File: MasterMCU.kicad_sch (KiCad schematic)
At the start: 0 parts

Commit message: STM32 pinout
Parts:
- added C201, C205, C206, C207, C208, C210, C212, C213, C214: 100n, Capacitor_SMD:C_0805_2012Metric, symbol Device:C
- added C202, C203, C216, C218: 6p, Capacitor_SMD:C_0805_2012Metric, symbol Device:C
- added C204: 10u, Capacitor_SMD:C_0805_2012Metric, symbol Device:C
- added C209, C211, C215, C217: 2u2, Capacitor_SMD:C_0805_2012Metric, symbol Device:C
- added FB201: 90R, Resistor_SMD:R_0805_2012Metric, symbol Device:FerriteBead
- added R201, R202: 100k, Resistor_SMD:R_0805_2012Metric, symbol Device:R_US
- added R203, R204, R205, R206: 22R, symbol Device:R_US
- added SW201: RST, Button_Switch_SMD:SW_SPST_B3U-1000P, symbol Switch:SW_SPST
- added SW202: BOOT, Button_Switch_SMD:SW_SPST_B3U-1000P, symbol Switch:SW_SPST
- added U201: STM32H7B0VBTx, Package_QFP:LQFP-100_14x14mm_P0.5mm, symbol MCU_ST_STM32H7:STM32H7B0VBTx
- added Y201: 16MHz, Crystal:Crystal_SMD_EuroQuartz_MT-4Pin_3.2x2.5mm, symbol Device:Crystal_GND24
- added Y202: 32.768kHZ, Crystal:Crystal_SMD_SeikoEpson_MC306-4Pin_8.0x3.2mm, symbol Device:Crystal_GND23
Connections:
- new net: R205.2, U201.3 (PE4)
- new net: R204.2, U201.1 (PE2)
- new net: C214.1, C215.1, FB201.1, U201.21 (VDDA)
- new net: C209.1, U201.48 (VCAP)
- new net: R206.2, U201.5 (PE6)
- new net: C211.1, U201.73 (VCAP)
- new net: R203.1, U201.78 (PC10)
- new net +3.3V: C204.1, C205.1, C206.1, C207.1, C208.1, C210.1, C212.1, C213.1, C217.1, FB201.2, R201.1, SW202.2 (B), U201.100 (VDD), U201.11 (VDD), U201.27 (VDD), U201.50 (VDD), U201.6 (VBAT), U201.75 (VDD)
- new net BCK_C: R203.2
- new net BOOT0: R202.1, SW202.1 (A), U201.94 (BOOT0)
- new net DOUT_C: U201.79 (PC11)
- new net GND: C201.2, C202.1, C203.1, C204.2, C205.2, C206.2, C207.2, C208.2, C209.2, C210.2, C211.2, C212.2, C213.2, C214.2, C215.2, C216.2, C217.2, C218.2, R202.2, SW201.1 (A), U201.10 (VSS), U201.19 (VSSA), U201.26 (VSS), U201.49 (VSS), U201.74 (VSS), U201.99 (VSS), Y201.2, Y201.4, Y202.2, Y202.3
- new net HSE_IN: C203.2, U201.12 (PH0), Y201.3
- new net HSE_OUT: C202.2, U201.13 (PH1), Y201.1
- new net LFE_IN: C216.1, U201.9 (PC15), Y202.1
- new net LFE_OUT: C218.1, U201.8 (PC14), Y202.4
- new net LORA_BUSY: U201.97 (PE0)
- new net LORA_IRQ: U201.98 (PE1)
- new net LORA_MISO: U201.4 (PE5)
- new net LORA_MOSI: R206.1
- new net LORA_NRST: U201.2 (PE3)
- new net LORA_SCK: R204.1, R205.1
- new net LRCK_C: U201.77 (PA15)
- new net NRST: C201.1, R201.2, SW201.2 (B), U201.14 (NRST)
- new net SWCLK: U201.76 (PA14)
- new net SWDIO: U201.72 (PA13)
- new net SWO: U201.36 (PB2)
- no-connect marks 0 -> 1
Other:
- note added: "Debug Header"
- note added: "HFE Crystal"
- note added: "LFE Crystal"
- note added: "MCU- STM32H7B0BVTx - LQFP100"

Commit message: peripheral schematic stuff
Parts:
- added RN201, RN203, RN204: 47R, symbol Device:R_Pack04
- added RN202: 15k, symbol Device:R_Pack04
- added SW203: SW_ADDR, symbol Switch:SW_DIP_x05
- R203: value 22R -> 15k
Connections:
- net +3.3V: now also R203.1, RN202.5 (R4.2), RN202.6 (R3.2), RN202.7 (R2.2), RN202.8 (R1.2)
- net BCK_C: now also RN204.3 (R3.1); no longer R203.2
- net GND: now also SW203.1, SW203.2, SW203.3, SW203.4, SW203.5
- net LRCK_C: now also RN204.4 (R4.1); no longer U201.77 (PA15)
- net +3.3VA: now reaches C214.1, C215.1, FB201.1, U201.21 (VDDA)
- net BATT: now reaches U201.24 (PA2)
- net WS_1: now reaches U201.28 (PA4)
- net WS_1: now also RN201.5 (R4.2)
- net CK_1: now reaches U201.29 (PA5)
- net CK_1: now also RN201.6 (R3.2)
- net DOUT_A: now reaches U201.30 (PA6)
- net MCK_1: now reaches U201.32 (PC4)
- net MCK_1: now also RN201.7 (R2.2)
- net WS_2: now reaches U201.51 (PB12)
- net WS_2: now also RN203.5 (R4.2)
- net CK_2: now reaches U201.52 (PB13)
- net CK_2: now also RN203.6 (R3.2)
- net DOUT_B: now reaches U201.53 (PB14)
- net MCK_2: now reaches U201.63 (PC6)
- net MCK_2: now also RN203.7 (R2.2)
- net MCK_3: now reaches U201.64 (PC7)
- net MCK_3: now also RN204.7 (R2.2)
- net CK_3: now reaches U201.78 (PC10)
- net CK_3: now also RN204.6 (R3.2); no longer R203.1
- net at U201.81 (PD0): now also R203.2, SW203.10
- net at U201.82 (PD1): now also RN202.4 (R4.1), SW203.9
- net at U201.83 (PD2): now also RN202.3 (R3.1), SW203.8
- net at U201.84 (PD3): now also RN202.2 (R2.1), SW203.7
- net at U201.85 (PD4): now also RN202.1 (R1.1), SW203.6
- new net BCK_A: RN201.3 (R3.1)
- new net BCK_B: RN203.3 (R3.1)
- new net LRCK_A: RN201.4 (R4.1)
- new net LRCK_B: RN203.4 (R4.1)
- new net MCK_A: RN201.2 (R2.1)
- new net MCK_B: RN203.2 (R2.1)
- new net MCK_C: RN204.2 (R2.1)
- new net WS_3: RN204.5 (R4.2), U201.77 (PA15)
- no-connect marks 1 -> 43

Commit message: SWD header
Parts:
- added D201: PMEG3030, Diode_SMD:D_SOD-123, symbol Device:D_Schottky
- added J201: SWD Header, Connector_PinHeader_2.54mm:PinHeader_1x06_P2.54mm_Vertical, symbol Connector:Conn_01x06_Pin
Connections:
- net +3.3V: now also D201.1 (K)
- net GND: now also J201.3 (Pin_3)
- net NRST: now also J201.5 (Pin_5)
- net SWCLK: now also J201.2 (Pin_2)
- net SWDIO: now also J201.4 (Pin_4)
- net SWO: now also J201.6 (Pin_6)
- new net: D201.2 (A), J201.1 (Pin_1)
- no-connect marks 43 -> 56
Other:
- moved on the sheet: RN201, RN203, RN204

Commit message: LEDs and footprints
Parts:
- added D202, D203, D204: LED, LED_SMD:LED_0805_2012Metric, symbol Device:LED
- added Q201, Q202, Q203: BC847, Package_TO_SOT_SMD:SOT-23, symbol Transistor_BJT:BC847
- added RN205: 15k, Resistor_SMD:R_Array_Concave_4x0402, symbol Device:R_Pack04
- added RN206: 330, Resistor_SMD:R_Array_Concave_4x0402, symbol Device:R_Pack04
- R203, R204, R205, R206: footprint (none) -> Resistor_SMD:R_0805_2012Metric
- RN201, RN202, RN203, RN204: footprint (none) -> Resistor_SMD:R_Array_Concave_4x0402
- SW203: footprint (none) -> Package_DIP:DIP-10_W7.62mm
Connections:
- net +3.3V: now also RN206.2 (R2.1), RN206.3 (R3.1), RN206.4 (R4.1)
- net +3.3VA: now also U201.20 (VREF+)
- net GND: now also Q201.2 (E), Q202.2 (E), Q203.2 (E)
- net ADDR_1: now reaches R203.2, SW203.10, U201.81 (PD0)
- net ADDR3: now reaches RN202.3 (R3.1), SW203.8, U201.83 (PD2)
- net ADDR_2: now reaches RN202.4 (R4.1), SW203.9, U201.82 (PD1)
- net at U201.55 (PD8): now also RN205.4 (R4.1)
- net at U201.56 (PD9): now also RN205.3 (R3.1)
- net at U201.57 (PD10): now also RN205.2 (R2.1)
- net BATT renamed +BATT
- new net: D202.1 (K), Q201.3 (C)
- new net: D202.2 (A), RN206.5 (R4.2)
- new net: D203.1 (K), Q202.3 (C)
- new net: D203.2 (A), RN206.6 (R3.2)
- new net: Q202.1 (B), RN205.6 (R3.2)
- new net: Q203.1 (B), RN205.5 (R4.2)
- new net: Q201.1 (B), RN205.7 (R2.2)
- new net: D204.1 (K), Q203.3 (C)
- new net: D204.2 (A), RN206.7 (R2.2)
- no-connect marks 56 -> 57

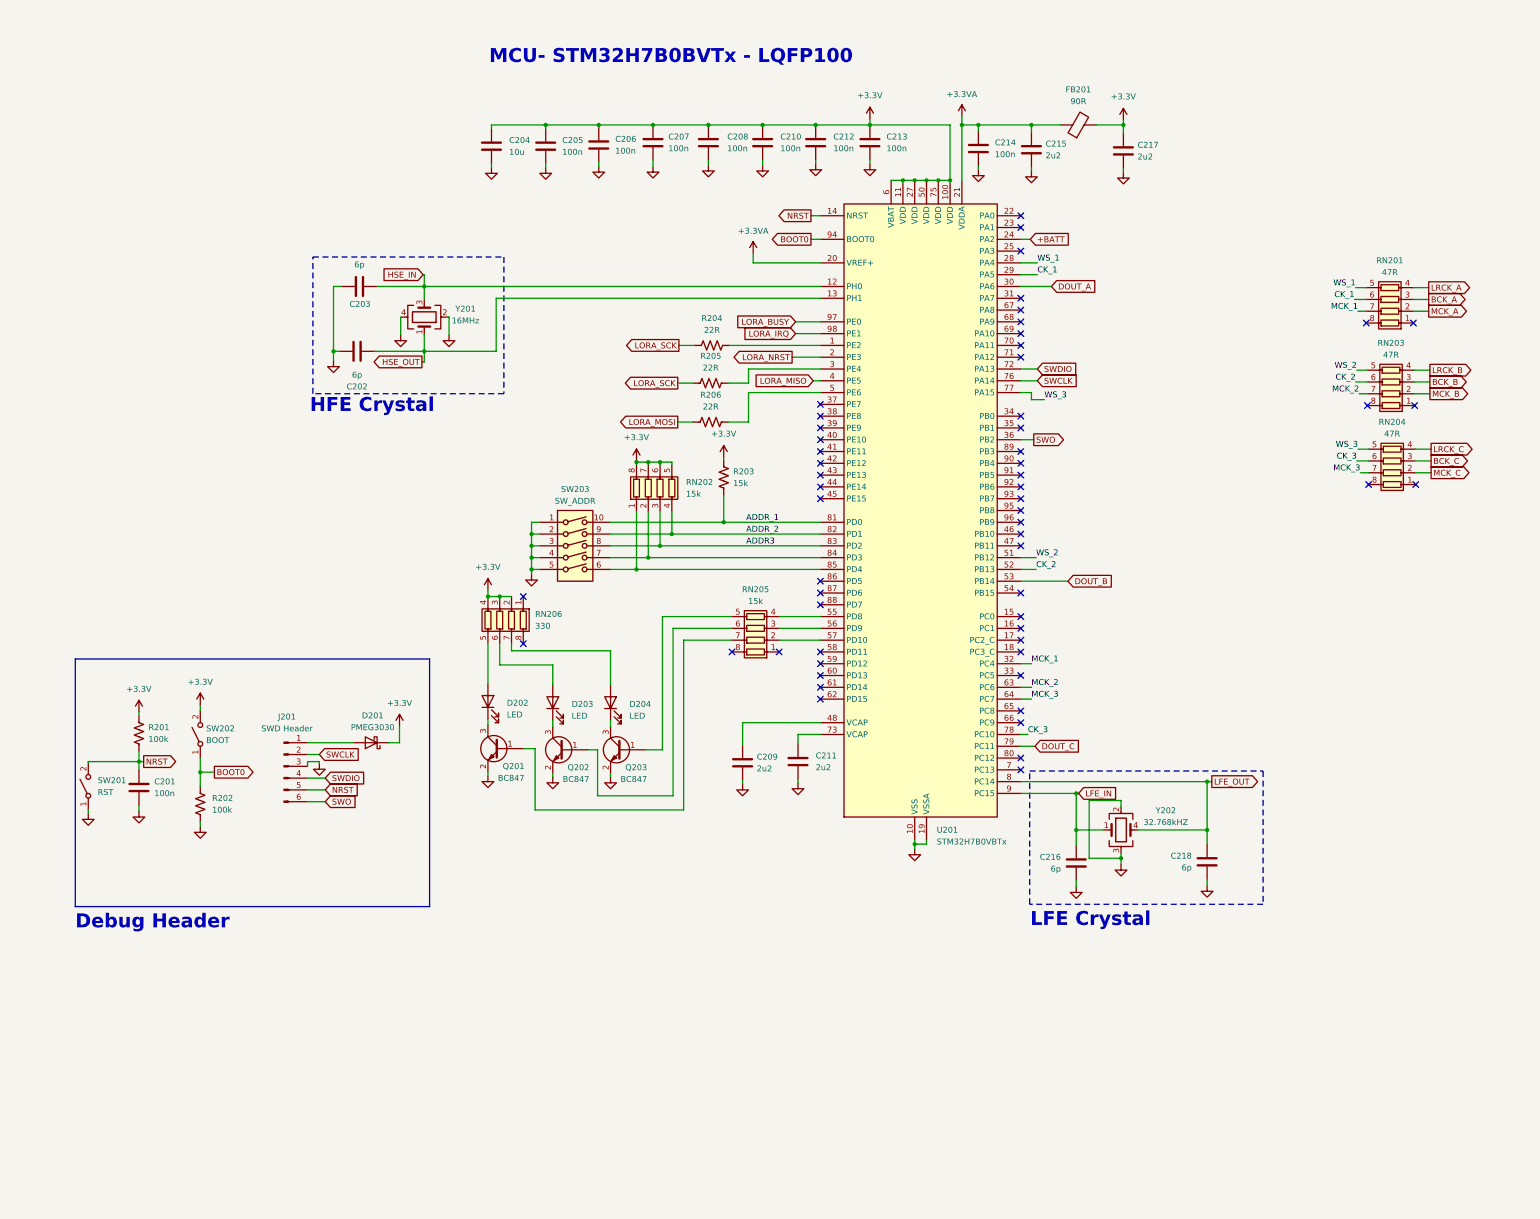
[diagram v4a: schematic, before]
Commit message: RF schematic drawn
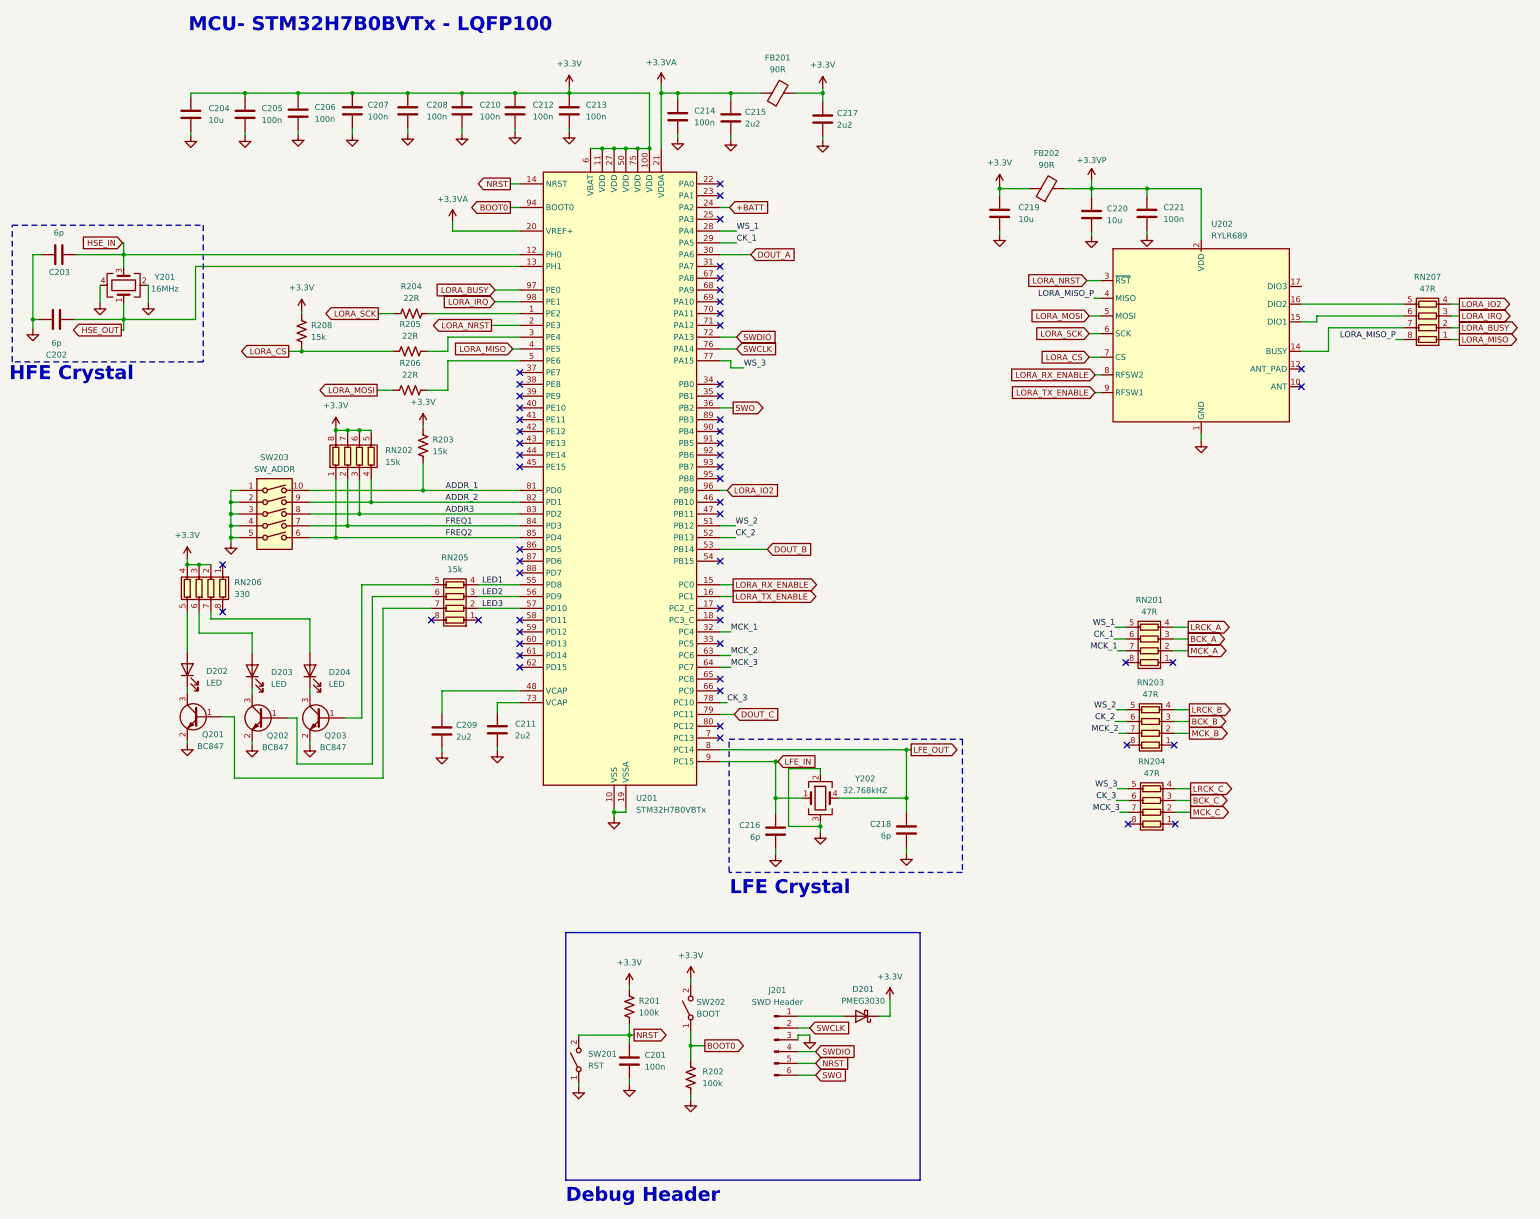
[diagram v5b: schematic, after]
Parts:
- added C219, C220: 10u, Capacitor_SMD:C_0805_2012Metric, symbol Device:C
- added C221: 100n, Capacitor_SMD:C_0805_2012Metric, symbol Device:C
- added FB202: 90R, Resistor_SMD:R_0805_2012Metric, symbol Device:FerriteBead
- added R208: 15k, Resistor_SMD:R_0805_2012Metric, symbol Device:R_US
- added RN207: 47R, Resistor_SMD:R_Array_Concave_4x0402, symbol Device:R_Pack04
- added U202: RYLR689, RF_Module:RYLR689, symbol RF_Module:RYLR689
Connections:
- net +3.3V: now also C219.1, FB202.1, R208.1
- net GND: now also C219.2, C220.2, C221.2, U202.1 (GND), U202.13 (GND), U202.18 (GND)
- net LORA_BUSY: now also RN207.2 (R2.1)
- net LORA_IRQ: now also RN207.3 (R3.1)
- net LORA_MISO: now also RN207.1 (R1.1)
- net LORA_MOSI: now also U202.5 (MOSI)
- net LORA_NRST: now also U202.3 (~{RST})
- net LORA_SCK: now also U202.6 (SCK); no longer R205.1
- net FREQ2: now reaches RN202.1 (R1.1), SW203.6, U201.85 (PD4)
- net FREQ1: now reaches RN202.2 (R2.1), SW203.7, U201.84 (PD3)
- net LED3: now reaches RN205.2 (R2.1), U201.57 (PD10)
- net LED2: now reaches RN205.3 (R3.1), U201.56 (PD9)
- net LED1: now reaches RN205.4 (R4.1), U201.55 (PD8)
- net LORA_RX_ENABLE: now reaches U201.15 (PC0)
- net LORA_RX_ENABLE: now also U202.8 (RFSW2)
- net LORA_TX_ENABLE: now reaches U201.16 (PC1)
- net LORA_TX_ENABLE: now also U202.9 (RFSW1)
- net LORA_IO2: now reaches U201.96 (PB9)
- net LORA_IO2: now also RN207.4 (R4.1)
- new net: RN207.7 (R2.2), U202.14 (BUSY)
- new net: RN207.6 (R3.2), U202.15 (DIO1)
- new net: RN207.5 (R4.2), U202.16 (DIO2)
- new net +3.3VP: C220.1, C221.1, FB202.2, U202.2 (VDD)
- new net LORA_CS: R205.1, R208.2, U202.7 (CS)
- new net LORA_MISO_P: RN207.8 (R1.2), U202.4 (MISO)
- no-connect marks 57 -> 56
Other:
- moved on the sheet: C201, C202, C203, C204, C205, C206, C207, C208, C209, C210, C211, C212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

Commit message: op amp input stage
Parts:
- RN201, RN202, RN203, RN204, RN205, RN206: footprint Resistor_SMD:R_Array_Concave_4x0402 -> Resistor_SMD:R_Array_Concave_4x0603
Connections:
- net BCK_A: now also RN201.1 (R1.1); no longer RN201.3 (R3.1)
- net BCK_B: now also RN203.1 (R1.1); no longer RN203.3 (R3.1)
- net BCK_C: now also RN204.1 (R1.1); no longer RN204.3 (R3.1)
- net CK_1: now also RN201.8 (R1.2); no longer RN201.6 (R3.2)
- net CK_2: now also RN203.8 (R1.2); no longer RN203.6 (R3.2)
- net CK_3: now also RN204.8 (R1.2); no longer RN204.6 (R3.2)
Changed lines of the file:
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@@
 	)
 	(no_connect
+		(at 262.636 179.578)
+	)
+	(no_connect
 		(at 175.006 134.874)
 	)
@@
 	)
 	(no_connect
-		(at 272.796 184.658)
-	)
-	(no_connect
 		(at 131.826 142.494)
 	)
@@
 	)
 	(no_connect
-		(at 262.382 166.878)
+		(at 262.382 161.798)
 	)
 	(no_connect
@@
 	)
 	(no_connect
+		(at 272.796 179.578)
+	)
+	(no_connect
 		(at 175.006 117.094)
 	)
@@
 	)
 	(no_connect
-		(at 272.542 166.878)
+		(at 272.542 161.798)
 	)
 	(no_connect
-		(at 273.05 201.676)
+		(at 273.05 196.596)
 	)
 	(no_connect
@@
 	)
 	(no_connect
-		(at 262.89 201.676)
+		(at 262.89 196.596)
 	)
 	(no_connect
@@
 	)
 	(no_connect
-		(at 262.636 184.658)
-	)
-	(no_connect
 		(at 175.006 63.754)
 	)
@@
 	(wire
 		(pts
-			(xy 259.842 161.798) (xy 262.382 161.798)
+			(xy 259.842 166.878) (xy 262.382 166.878)
 		)
 		(stroke
@@
 	(wire
 		(pts
-			(xy 260.35 196.596) (xy 262.89 196.596)
+			(xy 260.35 201.676) (xy 262.89 201.676)
 		)
 		(stroke
@@
 	(wire
 		(pts
-			(xy 272.542 161.798) (xy 275.844 161.798)
+			(xy 272.542 166.878) (xy 275.844 166.878)
 		)
 		(stroke
@@
 	(wire
 		(pts
-			(xy 273.05 196.596) (xy 276.352 196.596)
+			(xy 273.05 201.676) (xy 276.352 201.676)
 		)
 		(stroke
@@
 	(wire
 		(pts
-			(xy 260.096 179.578) (xy 262.636 179.578)
+			(xy 260.096 184.658) (xy 262.636 184.658)
 		)
 		(stroke
@@
 	(wire
 		(pts
-			(xy 272.796 179.578) (xy 276.098 179.578)
+			(xy 272.796 184.658) (xy 276.098 184.658)
 		)
 		(stroke
@@
 	)
 	(label "CK_1"
-		(at 259.842 161.798 180)
+		(at 259.842 166.878 180)
 		(fields_autoplaced yes)
 		(effects
@@
 	)
 	(label "CK_2"
-		(at 260.096 179.578 180)
+		(at 260.096 184.658 180)
 		(fields_autoplaced yes)
 		(effects
@@
 	)
 	(label "CK_3"
-		(at 260.35 196.596 180)
+		(at 260.35 201.676 180)
 		(fields_autoplaced yes)
 		(effects
@@
 	(global_label "BCK_C"
 		(shape output)
-		(at 276.352 196.596 0)
+		(at 276.352 201.676 0)
 		(fields_autoplaced yes)
 		(effects
@@
 		)
 		(property "Intersheetrefs" "${INTERSHEET_REFS}"
-			(at 285.3848 196.596 0)
+			(at 285.3848 201.676 0)
 			(effects
 				(font
@@
 	(global_label "BCK_A"
 		(shape output)
-		(at 275.844 161.798 0)
+		(at 275.844 166.878 0)
 		(fields_autoplaced yes)
 		(effects
@@
 		)
 		(property "Intersheetrefs" "${INTERSHEET_REFS}"
-			(at 284.6954 161.798 0)
+			(at 284.6954 166.878 0)
 			(effects
 				(font
@@
 	(global_label "BCK_B"
 		(shape output)
-		(at 276.098 179.578 0)
+		(at 276.098 184.658 0)
 		(fields_autoplaced yes)
 		(effects
@@
 		)
 		(property "Intersheetrefs" "${INTERSHEET_REFS}"
-			(at 285.1308 179.578 0)
+			(at 285.1308 184.658 0)
 			(effects
 				(font
@@
 			)
 		)
-		(property "Footprint" "Resistor_SMD:R_Array_Concave_4x0402"
+		(property "Footprint" "Resistor_SMD:R_Array_Concave_4x0603"
 			(at 117.856 145.669 90)
 			(effects
@@
 			)
 		)
-		(property "Footprint" "Resistor_SMD:R_Array_Concave_4x0402"
+		(property "Footprint" "Resistor_SMD:R_Array_Concave_4x0603"
 			(at 267.462 154.813 90)
 			(effects
@@
 			)
 		)
-		(property "Footprint" "Resistor_SMD:R_Array_Concave_4x0402"
+		(property "Footprint" "Resistor_SMD:R_Array_Concave_4x0603"
 			(at 104.267 122.428 90)
 			(effects
@@
 			)
 		)
-		(property "Footprint" "Resistor_SMD:R_Array_Concave_4x0402"
+		(property "Footprint" "Resistor_SMD:R_Array_Concave_4x0603"
 			(at 267.716 172.593 90)
 			(effects
@@
 		(on_board yes)
 		(dnp no)
-		(fields_autoplaced yes)
 		(property "Reference" "RN204"
 			(at 267.97 188.214 90)
@@
 			)
 		)
-		(property "Footprint" "Resistor_SMD:R_Array_Concave_4x0402"
+		(property "Footprint" "Resistor_SMD:R_Array_Concave_4x0603"
 			(at 267.97 189.611 90)
 			(effects
@@
 			)
 		)
-		(property "Footprint" "Resistor_SMD:R_Array_Concave_4x0402"
+		(property "Footprint" "Resistor_SMD:R_Array_Concave_4x0603"
 			(at 55.753 150.876 90)
 			(effects
